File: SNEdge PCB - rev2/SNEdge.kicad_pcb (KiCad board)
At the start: 2 copper layers, 40.8 x 18.4 mm, 33 parts, among them J10 R_O, J8 G_O, J9 B_O, U1 THS7376

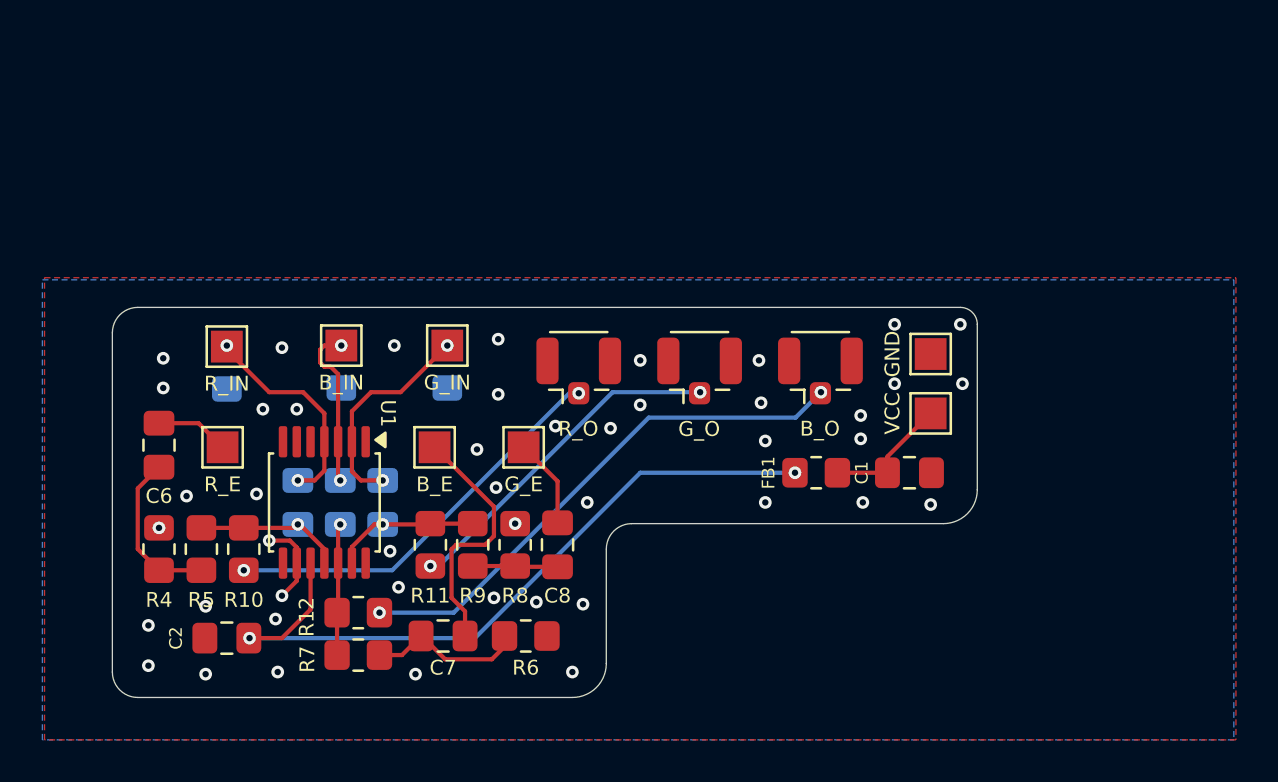
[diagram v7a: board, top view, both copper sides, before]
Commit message: Switch position of ferrite bead and bulk capacitor
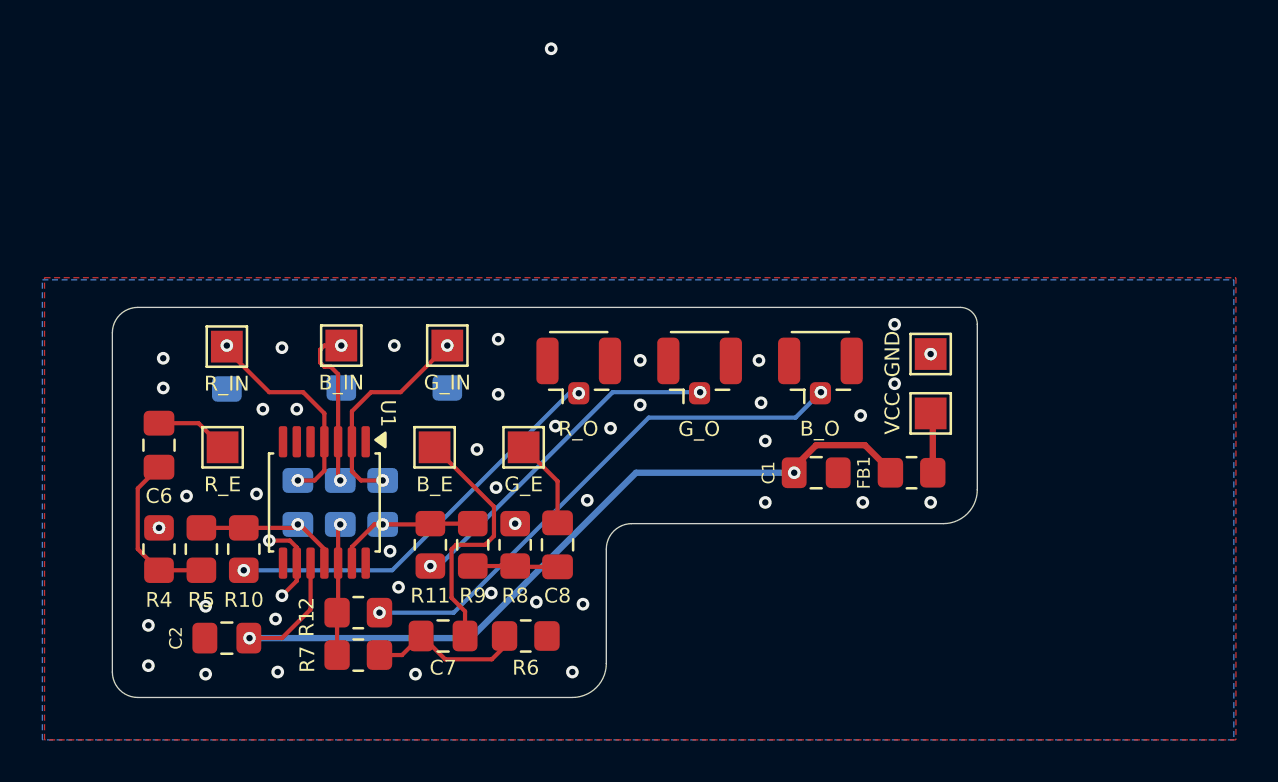
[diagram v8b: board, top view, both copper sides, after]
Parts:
- moved FB1 4.50 mm to (143.7, 98.2)
- moved C1 4.40 mm to (139.2, 98.2)
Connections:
- C1 pad 2: Net-(C1-Pad2) -> VCC
- FB1 pad 2: Net-(C1-Pad2) -> Net-(FB1-Pad2)
- TP1 pad 1: Net-(C1-Pad2) -> Net-(FB1-Pad2)
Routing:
- net Net-(C1-Pad2): track 6.01 -> 0.00 mm
- net VCC: track 34.6 -> 40.4 mm
- net Net-(FB1-Pad2): track 0.00 -> 2.84 mm
- net GND: vias 46 -> 44
- net (no net): vias 0 -> 1
